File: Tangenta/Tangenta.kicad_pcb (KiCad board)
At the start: 4 copper layers, 243.8 x 243.8 mm, 199 parts, among them J1 39281243, J10 1-2199230-5, J11 TYPEC-304-ACP16, J12 907-211A1019D10200, J13 906-151A1058D10200, J14 RC01133, J16 TF-115K, J17 2309410-1, J18 1-2199230-5, J19 HYC90-SIM06-180, J2 Conn_02x02_Top_Bottom, J3 10018784-10213TLF, J4 10018784-10213TLF, J5 HY911130A, J6 HY911130A, J7 HY911130A, J8 HDMI_19PIN_043, J9 HC-SFP-01L, Q1 2N7002, Q2 2N7002, Q3 2N7002, Q4 2N7002, U1 TPS54331DR, U10 TUSB321RWBR, U11 AOZ1353DI-01, U12 PUSB2X4Y-N, U13 LT8912B, U2 TPS54331DR, U3 TPS54331DR, U4 TPS54331DR, U5 74HC74D,653, U6 CD4060SA_TR, U7 74HC04D,653, U8 USB2514B-I_M2, U9 PUSB2X4Y-N, X1 X322524MOB4SI

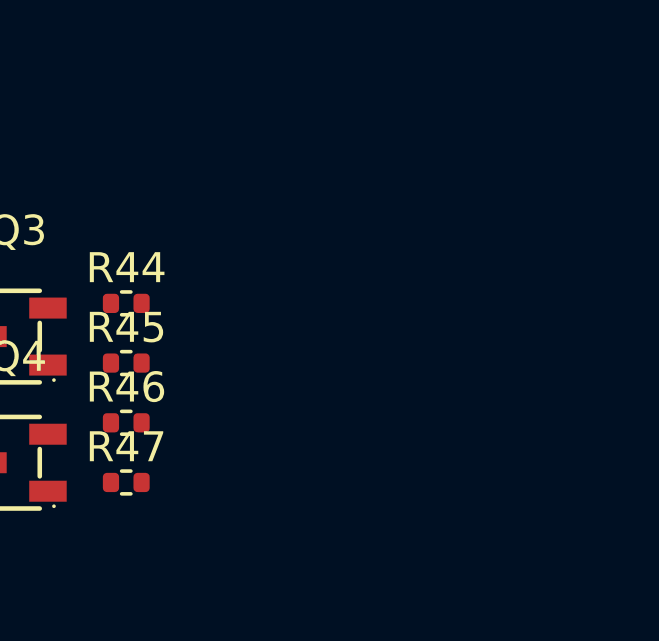
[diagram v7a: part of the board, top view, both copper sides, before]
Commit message: Finished HDMI schematic...
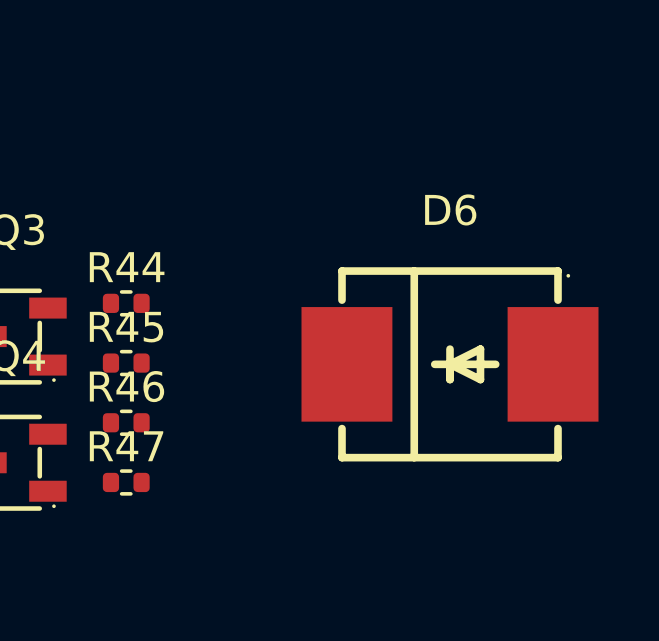
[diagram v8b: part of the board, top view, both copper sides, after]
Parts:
- added D6: B540C-13-F, B540C-13-F:B540C-13-F, F.Cu at (383.9, 98.2)
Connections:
- J8 pad 1: unconnected-(J8-TMDSData2+-Pad1) -> /DSI_HDMI/HDMI_TXD2_P
- J8 pad 10: unconnected-(J8-TMDSClock+-Pad10) -> /DSI_HDMI/HDMI_TXC_P
- J8 pad 11: unconnected-(J8-TMDSClockShield-Pad11) -> GNDREF
- J8 pad 12: unconnected-(J8-TMDSClock--Pad12) -> /DSI_HDMI/HDMI_TXC_N
- J8 pad 15: unconnected-(J8-SCL-Pad15) -> /DSI_HDMI/I2C_HDMI_SCL
- J8 pad 16: unconnected-(J8-SDA-Pad16) -> /DSI_HDMI/I2C_HDMI_SDA
- J8 pad 17: unconnected-(J8-DDC/CECGround-Pad17) -> GNDREF
- J8 pad 18: unconnected-(J8-+5VPower-Pad18) -> Net-(D6-K)
- J8 pad 19: unconnected-(J8-HotPlugDetect-Pad19) -> /DSI_HDMI/DSI.HPD
- J8 pad 2: unconnected-(J8-TMDSData2Shield-Pad2) -> GNDREF
- J8 pad 20: unconnected-(J8-EH-Pad20) -> /DSI_HDMI/CHASSIS
- J8 pad 3: unconnected-(J8-TMDSData2--Pad3) -> /DSI_HDMI/HDMI_TXD2_N
- J8 pad 4: unconnected-(J8-TMDSData1+-Pad4) -> /DSI_HDMI/HDMI_TXD1_P
- J8 pad 5: unconnected-(J8-TMDSData1Shield-Pad5) -> GNDREF
- J8 pad 6: unconnected-(J8-TMDSData1--Pad6) -> /DSI_HDMI/HDMI_TXD1_N
- J8 pad 7: unconnected-(J8-TMDSData0+-Pad7) -> /DSI_HDMI/HDMI_TXD0_P
- J8 pad 8: unconnected-(J8-TMDSData0Shield-Pad8) -> GNDREF
- J8 pad 9: unconnected-(J8-TMDSData0--Pad9) -> /DSI_HDMI/HDMI_TXD0_N
- U13 pad 21: unconnected-(U13A-HDMITX_CKN-Pad21) -> /DSI_HDMI/HDMI_TXC_N
- U13 pad 22: unconnected-(U13A-HDMITX_CKP-Pad22) -> /DSI_HDMI/HDMI_TXC_P
- U13 pad 24: unconnected-(U13A-HDMITX0_DN-Pad24) -> /DSI_HDMI/HDMI_TXD0_N
- U13 pad 25: unconnected-(U13A-HDMITX0_DP-Pad25) -> /DSI_HDMI/HDMI_TXD0_P
- U13 pad 27: unconnected-(U13A-HDMITX1_DN-Pad27) -> /DSI_HDMI/HDMI_TXD1_N
- U13 pad 28: unconnected-(U13A-HDMITX1_DP-Pad28) -> /DSI_HDMI/HDMI_TXD1_P
- U13 pad 30: unconnected-(U13A-HDMITX2_DN-Pad30) -> /DSI_HDMI/HDMI_TXD2_N
- U13 pad 31: unconnected-(U13A-HDMITX2_DP-Pad31) -> /DSI_HDMI/HDMI_TXD2_P
